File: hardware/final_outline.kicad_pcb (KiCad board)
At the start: 2 copper layers, 99.5 x 75 mm, 48 parts, among them P001 CANCONNECTOR, P002 CONN_01X14, P100 ISP, P101 DEBUG_LED, U401 MCP2551-I/SN, U403 LPC11C14, U501 MCP1755-33, U502 MCP1755-5, U503 Zsr1000gta, U6 TCA9543A, U7 LTC2943, U8 LTC2943

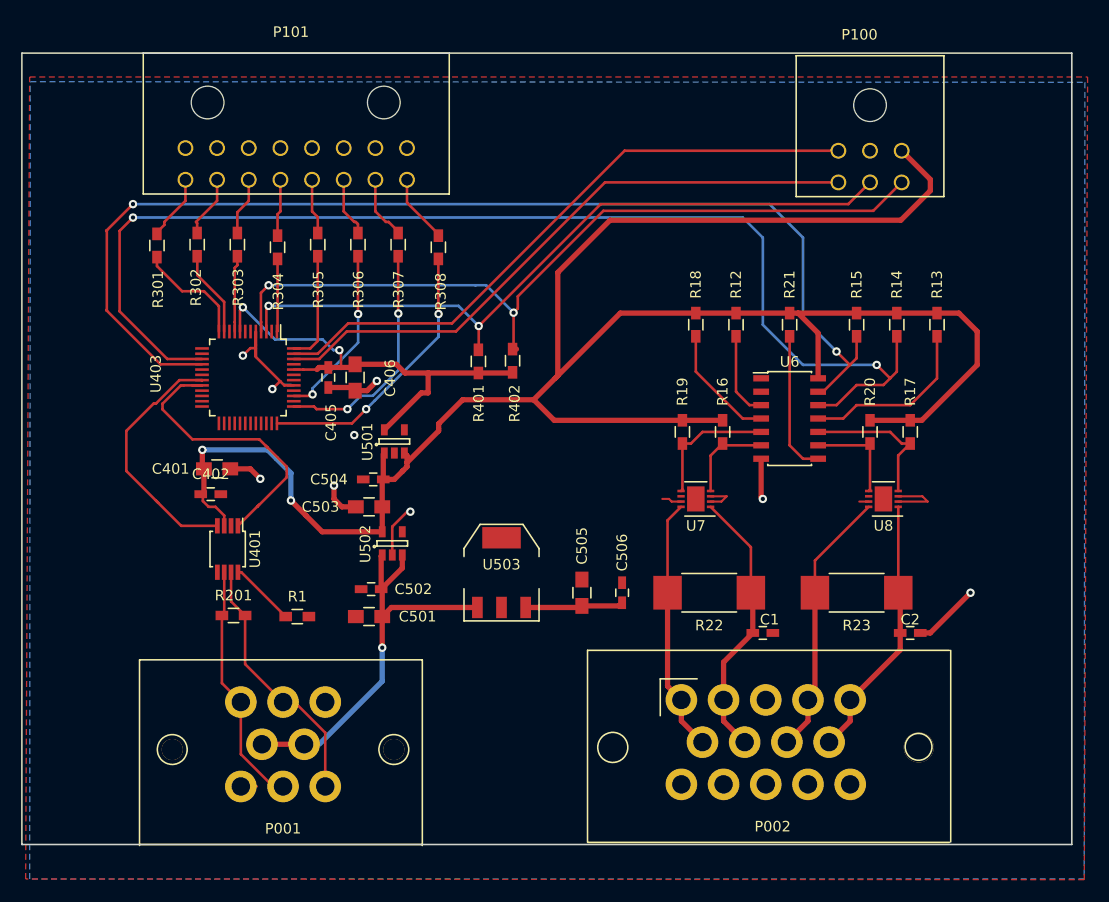
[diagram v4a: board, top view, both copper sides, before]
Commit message: Fixed multiple PCB issues.
Fixed track widths.
Added decoupling capacitor for multiplexer.
Added additional vias to ground plane.
Replaced traces with zones for high current connector inputs.
Added additional input for sense input and ground input to connector.
Removed 10V voltage regualator and associated circuitry.
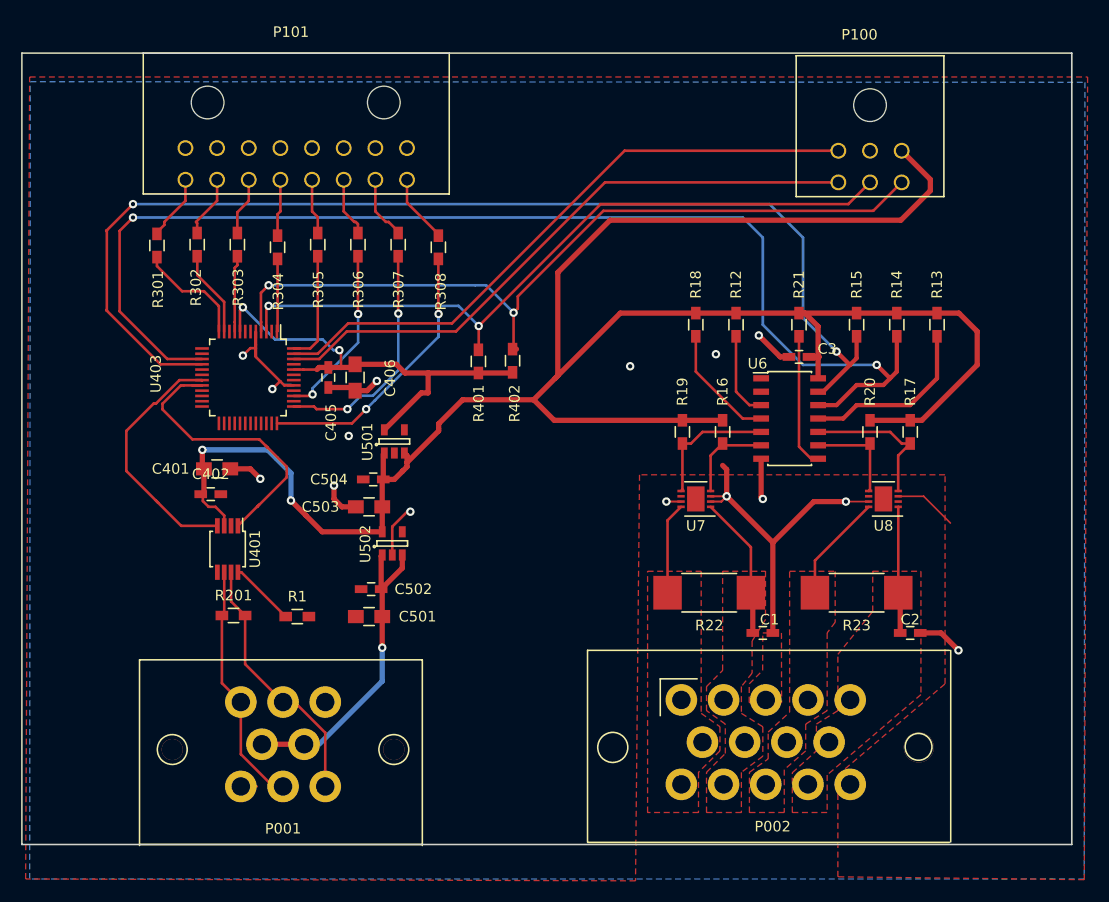
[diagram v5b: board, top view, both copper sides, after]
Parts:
- removed C505: 10μ, Capacitors_SMD:C_0805_HandSoldering
- removed C506: .1μ, Capacitors_SMD:C_0603_HandSoldering
- removed U503: Zsr1000gta, TO_SOT_Packages_SMD:SOT-223
- added C3: 0.1uF, Capacitors_SMD:C_0603_HandSoldering, F.Cu at (176.1, 81.8)
- R201: value R -> 120
- moved R21 0.89 mm to (176.1, 78.7)
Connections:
- P002 pad 10: Net-(P002-Pad10) -> /BACK_PANEL/CS_SENSE-
- P002 pad 11: Net-(P002-Pad11) -> /BACK_PANEL/CS_SENSE+
- P002 pad 12: Net-(P002-Pad12) -> /BACK_PANEL/LV_SENSE-
- P002 pad 13: Net-(P002-Pad13) -> /BACK_PANEL/LV_SENSE+
- P002 pad 14: Net-(P002-Pad14) -> GND
- P002 pad 3: Net-(P002-Pad3) -> GND
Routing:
- net GND: track 52.1 -> 81.1 mm, vias 8 -> 15
- net /BACK_PANEL/CS_SENSE-: track 25.8 -> 10.3 mm
- net /BACK_PANEL/LV_SENSE-: track 24.6 -> 10.2 mm
- net /BACK_PANEL/LV_SENSE+: track 25.2 -> 12.0 mm
- net /BACK_PANEL/CS_SENSE+: track 25.9 -> 13.6 mm
- net +12V: track 39.5 -> 30.1 mm
- net VCC: track 9.33 -> 0.00 mm
- net Net-(R21-Pad2): track 13.6 -> 12.6 mm
- net +5V: track 197.7 -> 198.5 mm
- net (no net): track 0.75 -> 0.63 mm, vias 1 -> 0
- added copper zone on F.Cu, net /BACK_PANEL/CS_SENSE+
- added copper zone on F.Cu, net /BACK_PANEL/CS_SENSE-
- added copper zone on F.Cu, net /BACK_PANEL/LV_SENSE+
- added copper zone on F.Cu, net /BACK_PANEL/LV_SENSE-
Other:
- net class Default: clearance 0.2 -> 0.13
- net class POWER: clearance 0.2 -> 0.13
- rule trace_clearance: 0.2 -> 0.13
